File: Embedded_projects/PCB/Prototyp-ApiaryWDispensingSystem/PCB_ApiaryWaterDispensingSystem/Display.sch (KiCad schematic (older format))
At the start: 1 part

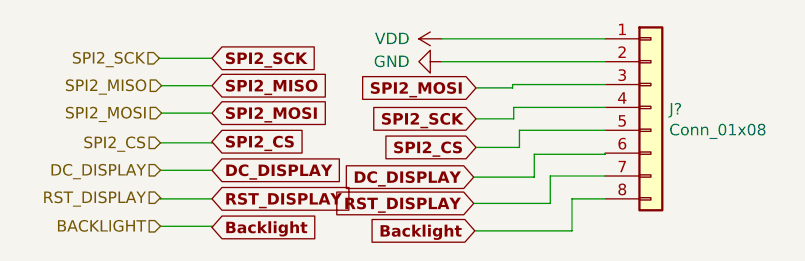
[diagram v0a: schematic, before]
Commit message: All signal has been routed, the analog part needs to be completed
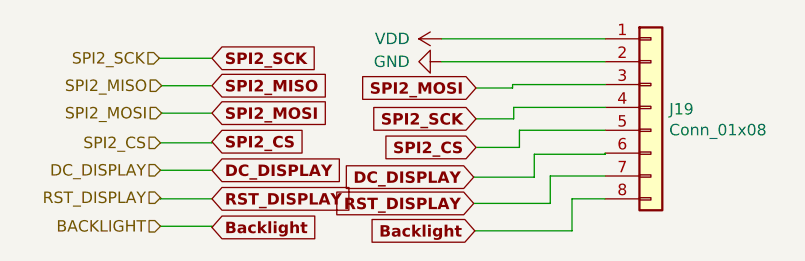
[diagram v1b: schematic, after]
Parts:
- J19: renamed from J?; footprint (none) -> Connector_PinSocket_2.54mm:PinSocket_1x08_P2.54mm_Vertical
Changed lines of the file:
@@
 SPI2_CS
 $Comp
-L power:VDD #PWR?
+L power:VDD #PWR032
 U 1 1 690ADEF2
 P 2390 900
-F 0 "#PWR?" H 2390 750 50  0001 C CNN
+F 0 "#PWR032" H 2390 750 50  0001 C CNN
 F 1 "VDD" V 2390 1040 50  0000 L CNN
 F 2 "" H 2390 900 50  0001 C CNN
@@
 $EndComp
 $Comp
-L power:GND #PWR?
+L power:GND #PWR033
 U 1 1 690AE5BB
 P 2390 1000
-F 0 "#PWR?" H 2390 750 50  0001 C CNN
+F 0 "#PWR033" H 2390 750 50  0001 C CNN
 F 1 "GND" V 2390 860 50  0000 R CNN
 F 2 "" H 2390 1000 50  0001 C CNN
@@
 Backlight
 $Comp
-L Connector_Generic:Conn_01x08 J?
+L Connector_Generic:Conn_01x08 J19
 U 1 1 690B007B
 P 3305 1200
-F 0 "J?" H 3385 1192 50  0000 L CNN
+F 0 "J19" H 3385 1192 50  0000 L CNN
 F 1 "Conn_01x08" H 3385 1101 50  0000 L CNN
-F 2 "" H 3305 1200 50  0001 C CNN
+F 2 "Connector_PinSocket_2.54mm:PinSocket_1x08_P2.54mm_Vertical" H 3305 1200 50  0001 C CNN
 F 3 "~" H 3305 1200 50  0001 C CNN
 	1    3305 1200
